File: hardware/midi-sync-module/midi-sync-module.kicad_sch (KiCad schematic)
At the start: 41 parts, among them J1 AudioJack2_SwitchT, J2 Conn_01x10_Male, J3 DIN-5_180degree, J4 Conn_02x05_Odd_Even, J5 Conn_02x05_Odd_Even, J6 Conn_01x16_Pin, Q1 MMBT3904, U1 ISU0205S05, U2 6N137, U3 ADP7142AUJZ-3.3

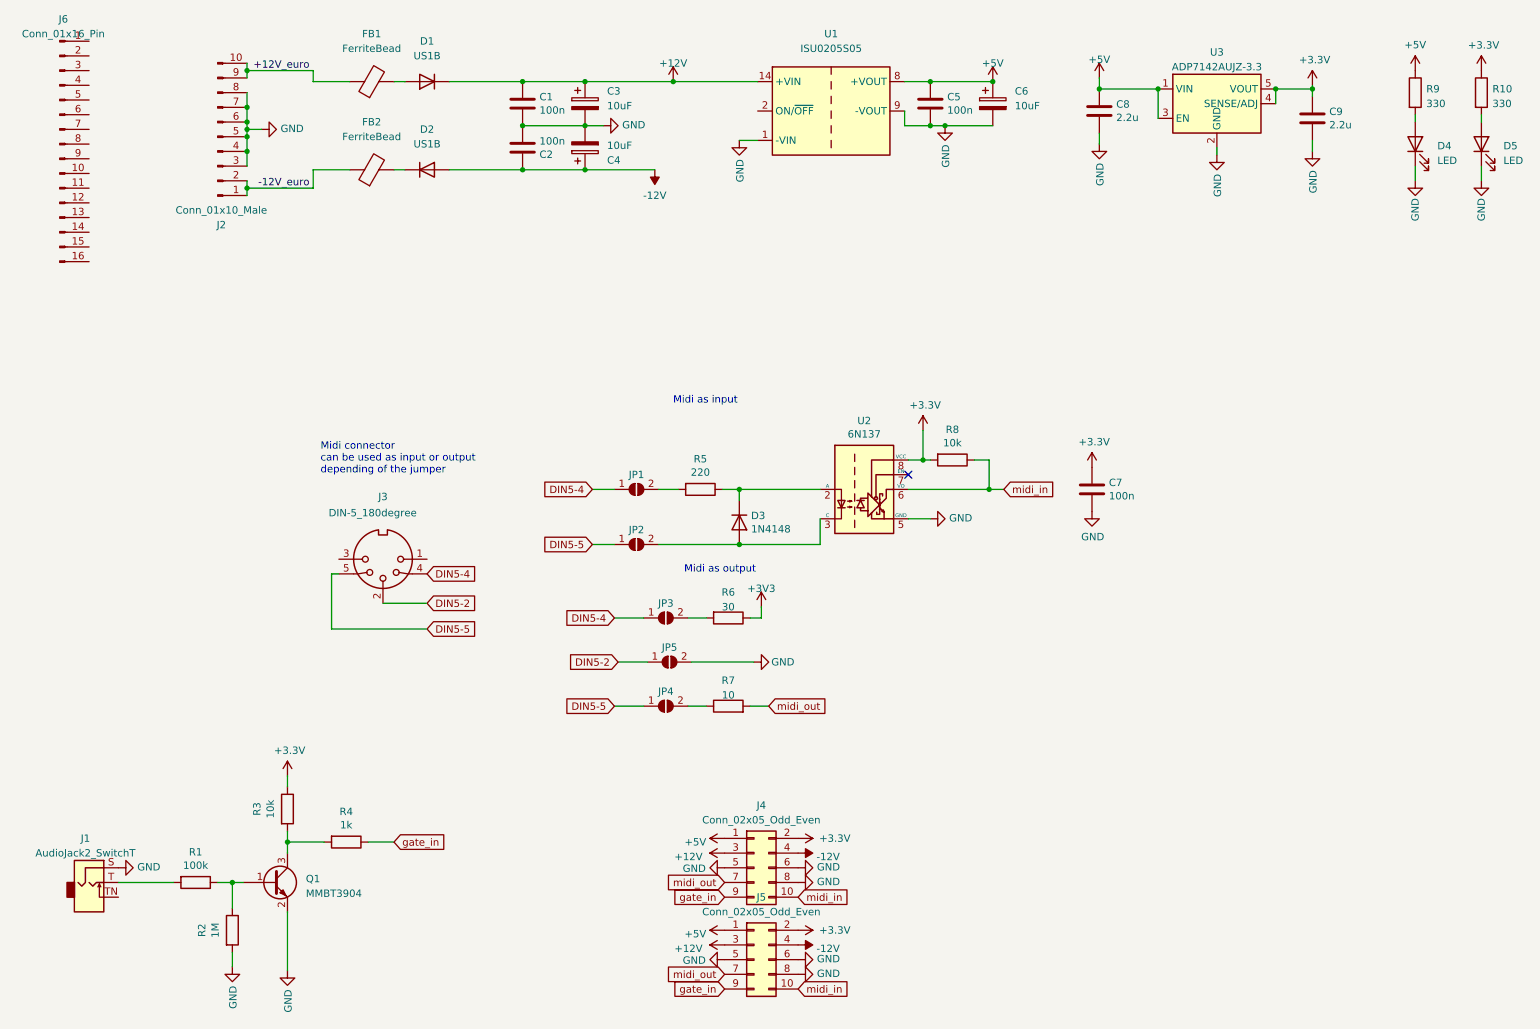
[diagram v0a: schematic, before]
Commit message: update pbc to v0.0.2 (fix polarized cap C3 and some texts) and panel c
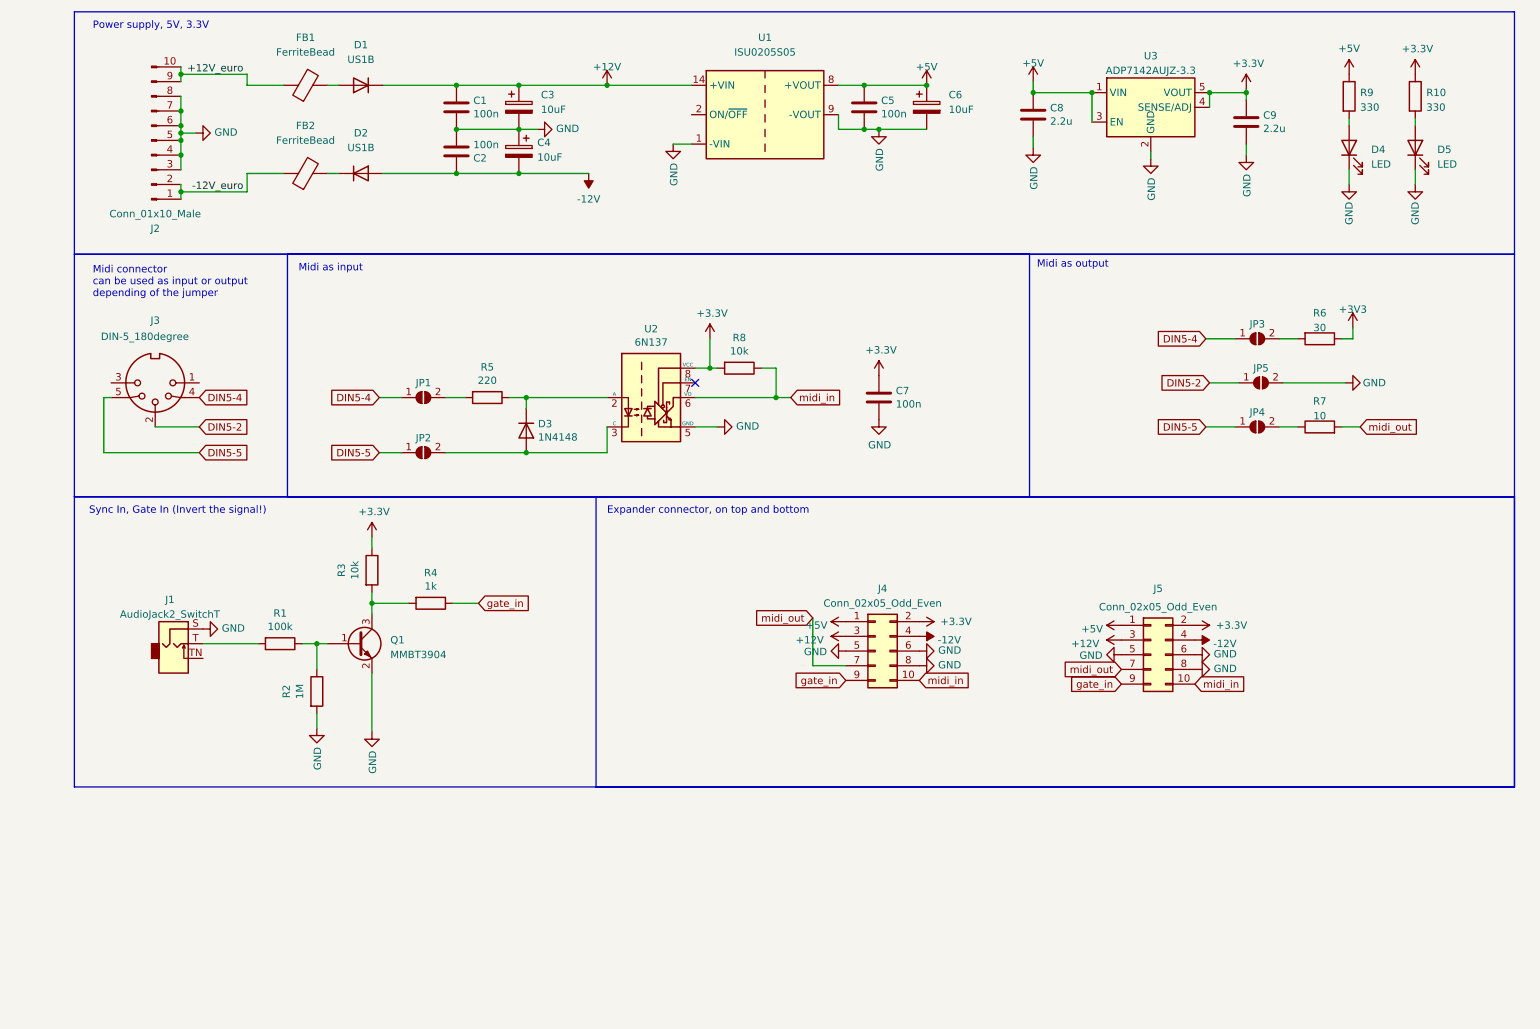
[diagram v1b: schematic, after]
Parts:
- removed J6: Conn_01x16_Pin, Connector_PinHeader_2.54mm:PinHeader_2x08_P2.54mm_Vertical, symbol Connector:Conn_01x16_Pin
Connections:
- net -12V: now also C4.2; no longer C4.1
- net GND: now also C4.1; no longer C4.2
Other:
- note added: "Expander connector, on top and bottom"
- note added: "Power supply, 5V, 3.3V"
- note added: "Sync In, Gate In (Invert the signal!)"
- company: (none) -> Lucas Bonvin
- title: (none) -> MIDI-sync-power-dev-board
- moved on the sheet: C1, C2, C3, C5, C6, C7, C8, C9, D1, D2, D3, D4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
